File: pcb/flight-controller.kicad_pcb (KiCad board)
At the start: 2 copper layers, 50 x 50 mm, 23 parts, among them IC1 ATMEGA32-A, K1 CONN_3, K10 CONN_3, K2 CONN_3, K3 CONN_3, K4 CONN_3, K5 CONN_3, K6 CONN_3, K7 CONN_3, K8 CONN_3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

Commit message: lots of improvements to flight control and PCB
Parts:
- added C10: 10uF, SM0805, F.Cu at (139.5, 90.5)
- added C11: 0.1uF, SM0603, F.Cu at (144.0, 106.5)
- added C12: 100nF, SM0603, F.Cu at (140.0, 92.8)
- added C13: 0.01uF, SM0603, F.Cu at (144.2, 112.2)
- added C5: 100nF, SM0603, F.Cu at (132.0, 101.2)
- added C7: 100nF, SM0603, F.Cu at (110.8, 101.5)
- added C8: 100nF, SM0603, F.Cu at (121.8, 94.2)
- added C9: 1uF, SM0603, F.Cu at (137.2, 92.8)
- added R4: 10k, SM0603, F.Cu at (112.2, 101.5)
- C1, C2: value C -> 22pF; footprint SM0402 -> SM0603
- C3: value C -> 2200pF; footprint SM0402 -> SM0603
- C4: value C -> 10nF; footprint SM0402 -> SM0603
- C6: value C -> 0.1uF; footprint SM0402 -> SM0603
- R1, R2, R3: value R -> 4.7k; footprint SM0402 -> SM0603
- X1: value CRYSTAL -> 16MHz; footprint SM0805 -> MADW__HC49U-S
- moved C1 8.27 mm to (106.2, 116.0), turned to 90 degrees
- moved C2 7.70 mm to (111.2, 116.0), turned to 90 degrees
- moved R3 3.18 mm to (141.5, 114.0), turned to 0 degrees
- moved P1 2.92 mm to (104.0, 101.0), turned to 90 degrees
- moved X1 2.80 mm to (108.8, 111.2), turned to 180 degrees
- moved R1 1.52 mm to (136.0, 112.8)
- moved C6 1.12 mm to (141.5, 112.2), turned to 0 degrees
- moved C3 0.79 mm to (140.8, 102.0)
- moved R2 0.79 mm to (136.0, 111.0)
- moved C4 0.56 mm to (142.0, 96.5)
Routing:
- net +3.3V: track 25.3 -> 60.3 mm
- net GND: track 254.1 -> 288.7 mm
- net +5V: track 100.9 -> 127.2 mm
- net N-0000039: track 11.6 -> 20.8 mm
- net N-0000020: track 11.9 -> 16.7 mm, vias 1 -> 0
- net N-0000017: track 0.00 -> 4.14 mm
- net N-0000030: track 2.88 -> 6.28 mm
- net /RESET: track 16.3 -> 13.3 mm
- net N-000006: track 26.0 -> 28.4 mm
- net N-0000044: track 15.7 -> 13.5 mm, vias 0 -> 1
- net N-0000057: track 12.7 -> 14.8 mm
- net N-000008: track 15.1 -> 17.0 mm
- net N-0000037: track 13.8 -> 12.5 mm, vias 1 -> 0
- net N-0000029: track 2.99 -> 4.03 mm
- net N-000003: track 19.8 -> 20.9 mm
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
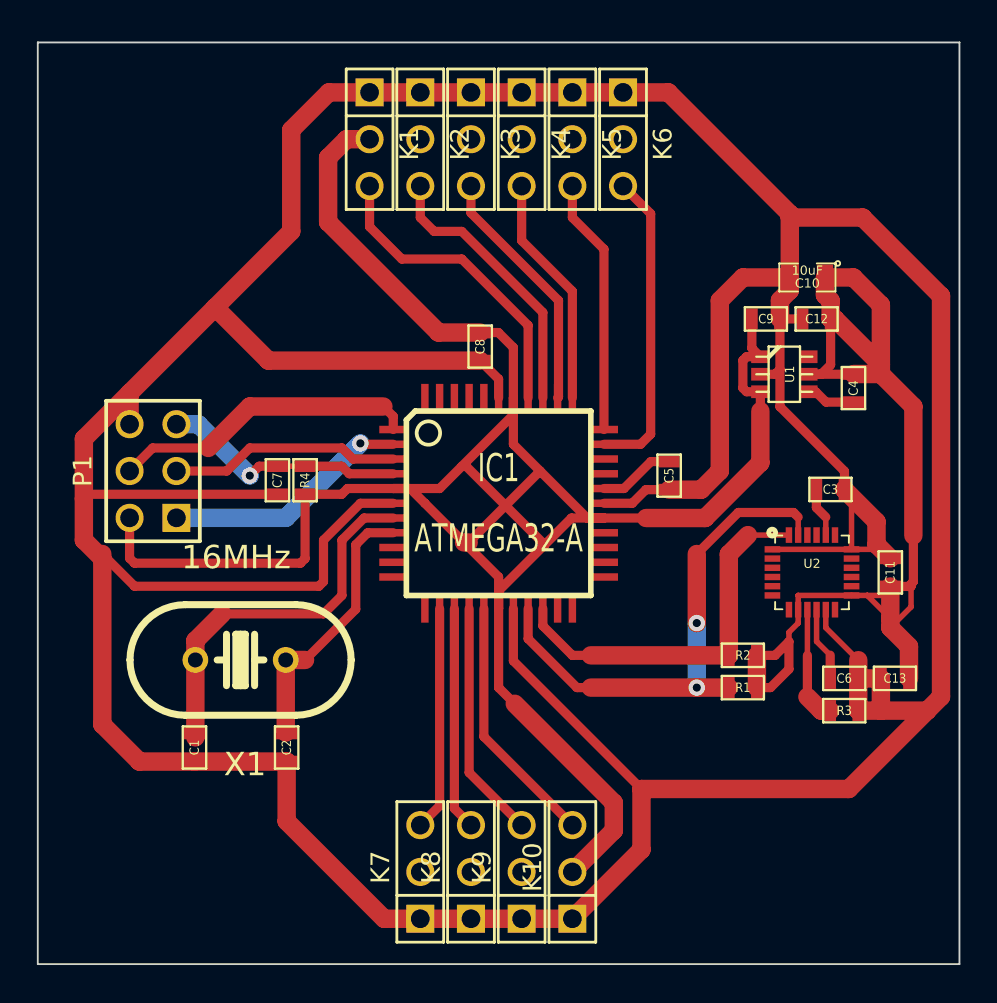
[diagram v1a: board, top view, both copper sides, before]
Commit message: finish yaw control, tune altitude correction
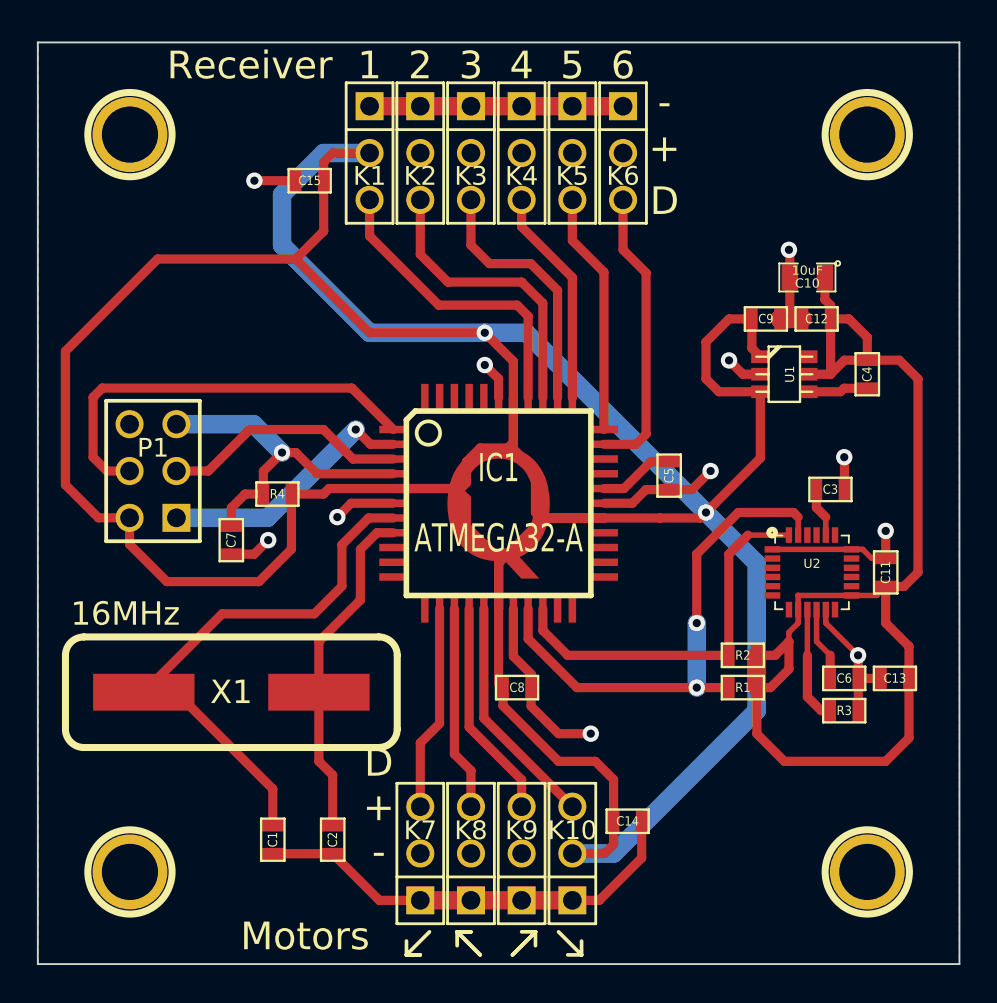
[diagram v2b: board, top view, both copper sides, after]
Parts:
- added ?: P***, 1pin, F.Cu at (142.8, 82.8)
- added ?: P***, 1pin, F.Cu at (142.8, 122.8)
- added ?: P***, 1pin, F.Cu at (102.8, 82.8)
- added ?: P***, 1pin, F.Cu at (102.8, 122.8)
- added C14: 100nF, SM0603, F.Cu at (129.8, 120.0)
- added C15: 100nF, SM0603, F.Cu at (112.5, 85.2)
- X1: footprint MADW__HC49U-S -> CRYSTAL-HC49-US
- moved C8 18.6 mm to (123.8, 112.8), turned to 180 degrees
- moved C1 6.56 mm to (110.5, 121.0)
- moved C2 5.59 mm to (113.8, 121.0)
- moved C7 4.10 mm to (108.2, 104.8)
- moved X1 1.82 mm to (108.2, 113.0)
- moved R4 1.68 mm to (110.8, 102.2), turned to 0 degrees
- moved C4 1.06 mm to (142.8, 95.8)
- moved K10 1.00 mm to (126.8, 121.8)
- moved K7 1.00 mm to (118.5, 121.8)
- moved K8 1.00 mm to (121.2, 121.8)
- moved K9 1.00 mm to (124.0, 121.8)
- moved K1 0.75 mm to (115.8, 83.8)
- moved K2 0.75 mm to (118.5, 83.8)
- moved K3 0.75 mm to (121.2, 83.8)
- moved K4 0.75 mm to (124.0, 83.8)
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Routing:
- net GND: track 288.7 -> 88.4 mm, vias 0 -> 11
- net +5V: track 127.2 -> 217.8 mm, vias 0 -> 2
- net N-0000037: track 20.8 -> 29.9 mm
- net N-0000024: track 16.7 -> 23.0 mm
- net /RESET: track 13.3 -> 18.6 mm
- net +3.3V: track 60.3 -> 64.1 mm
- net N-0000057: track 14.8 -> 18.4 mm
- net N-0000013: track 16.8 -> 15.7 mm
- net N-0000049: track 12.9 -> 11.9 mm
- net N-000003: track 12.1 -> 11.1 mm
- net N-000002: track 12.2 -> 11.2 mm
- net N-0000015: track 13.7 -> 12.7 mm
- net N-0000035: track 12.5 -> 13.4 mm
- net N-0000012: track 13.9 -> 13.2 mm
- net N-0000011: track 12.6 -> 11.9 mm
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- added copper zone on B.Cu, net GND
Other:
- board text added: "+"
- board text added: "-"
- board text added: "1"
- board text added: "2"
- board text added: "3"
- board text added: "4"
- board text added: "5"
- board text added: "6"
- board text added: "D"
- board text added: "D + -"
- board text added: "Flight Controller v0.2"
- board text added: "Motors"
- board text added: "Q"
- board text added: "Receiver"
